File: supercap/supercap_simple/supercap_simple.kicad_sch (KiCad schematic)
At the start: 48 parts, among them J1 Conn_01x02, J2 Conn_01x02, J4 Conn_01x02, J5 Conn_01x02

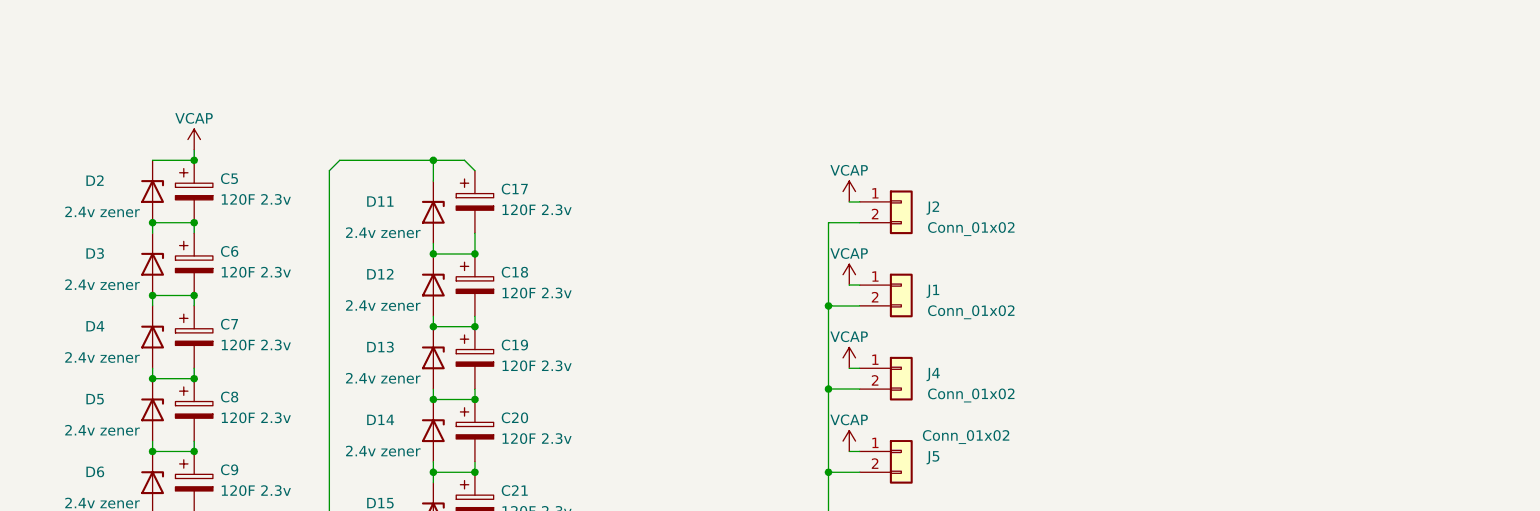
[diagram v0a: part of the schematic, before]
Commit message: Updated board files for July 2024 order. Added supercap_simple.
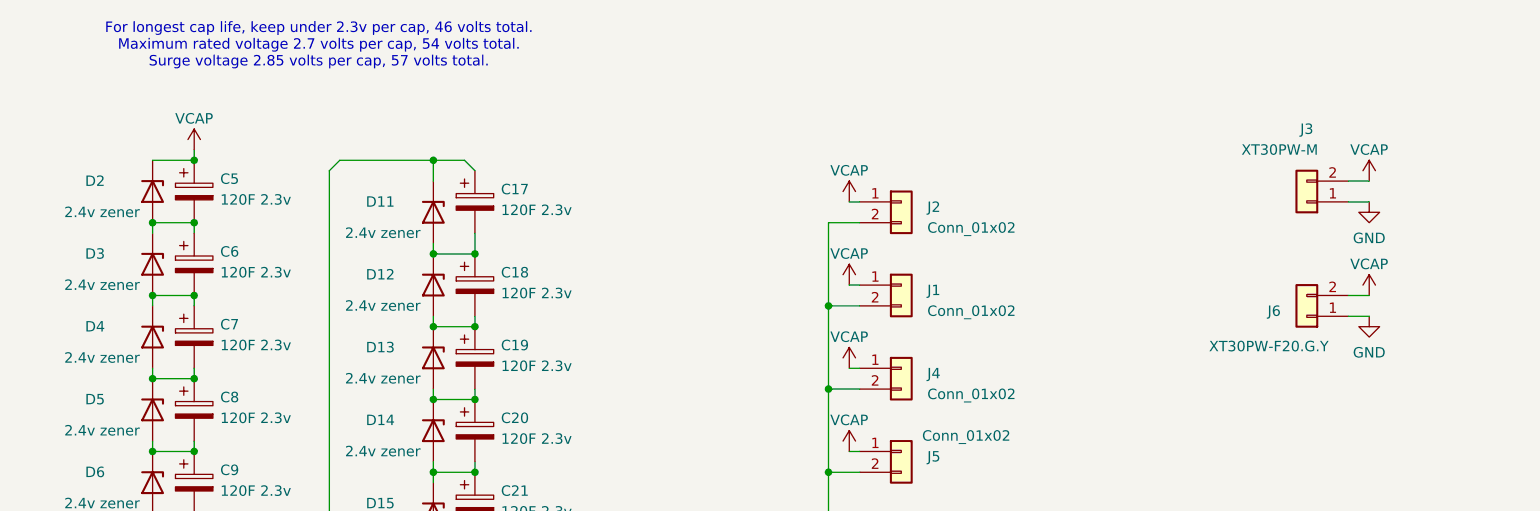
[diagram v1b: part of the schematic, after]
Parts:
- added J3: XT30PW-M, Connector_AMASS:AMASS_XT30PW-M_1x02_P2.50mm_Horizontal, symbol Connector_Generic:Conn_01x02
- added J6: XT30PW-F20.G.Y, Connector_AMASS:AMASS_XT30PW-F_1x02_P2.50mm_Horizontal, symbol Connector_Generic:Conn_01x02
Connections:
- net GND: now also J3.1 (Pin_1), J6.1 (Pin_1)
- net VCAP: now also J3.2 (Pin_2), J6.2 (Pin_2)
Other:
- note added: "For longest cap life, keep under 2.3v per cap, 46 volts total. Maximum rated voltage 2.7 volts per cap, 54 volts total. Surge voltage 2.85 volts per cap, 57 volts total."
